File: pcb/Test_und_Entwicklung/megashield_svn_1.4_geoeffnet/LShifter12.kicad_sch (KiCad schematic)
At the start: 3 parts, among them Q34 BSS138

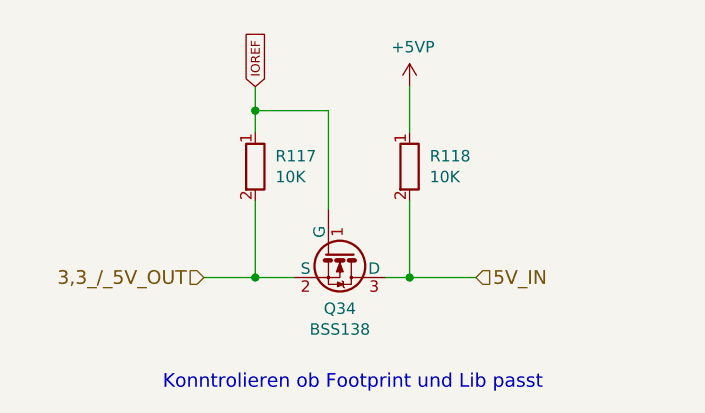
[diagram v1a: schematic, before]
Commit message: megashield_svn_1.4_geoeffnet
megashield_svn_1.4_geoeffnet
33 Q5-Q11,Q30-Q37 neue JLCPCB Nummer und neue Herstellernummer BSS138 (2n7002)
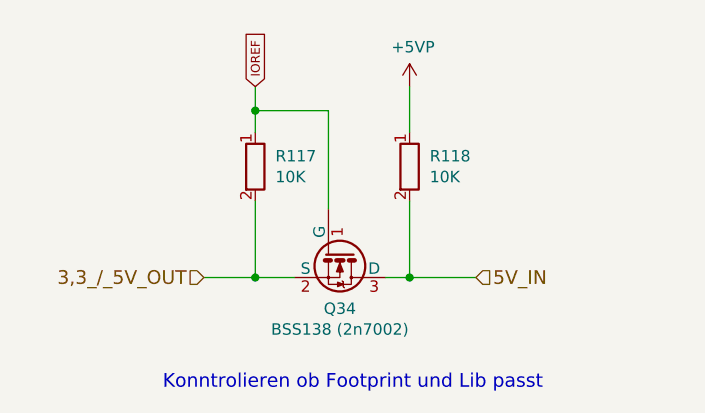
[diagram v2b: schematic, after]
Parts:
- Q34: value BSS138 -> BSS138 (2n7002); JLCPCB Basic / Extern 1 -> (none); JLCPCB LCSC Part C426569 -> C8545

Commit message: megashield_svn_1.4_geoeffnet
megashield_svn_1.4_geoeffnet
41 Q24 + R6 hinzugefügt und Summer ansteuerung umgeändert
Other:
- company: ML AG JL UZ -> ML AG JL BS UZ
